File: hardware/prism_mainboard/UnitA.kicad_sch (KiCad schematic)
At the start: 8 parts, among them U1 XC7Z010-1CLG400C

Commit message: KiCAD Update
Added Power System Schematics. Decided on a 4 in 1 Buck and LDO, LP87222TQ1, for 3.3V and 1.8V LDO, and 1.8V and 1.0V Buck converter.
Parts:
- U1: footprint CLG400_XIL -> XC7Z010-1CLG400C:CLG400_XIL

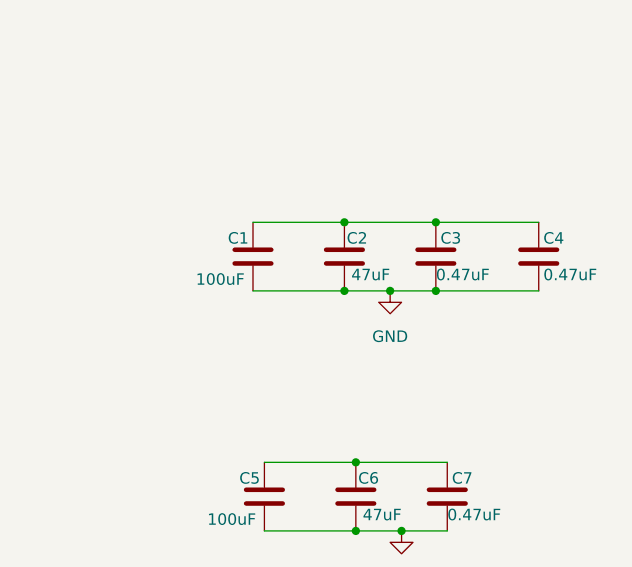
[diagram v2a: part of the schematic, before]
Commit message: Schematics
More schematics updates, moving to Desktop for editing. Continued with power usage, debating use of Dedicated DDR3/3L power IC instead of using LDO and Buck from mainboard power.
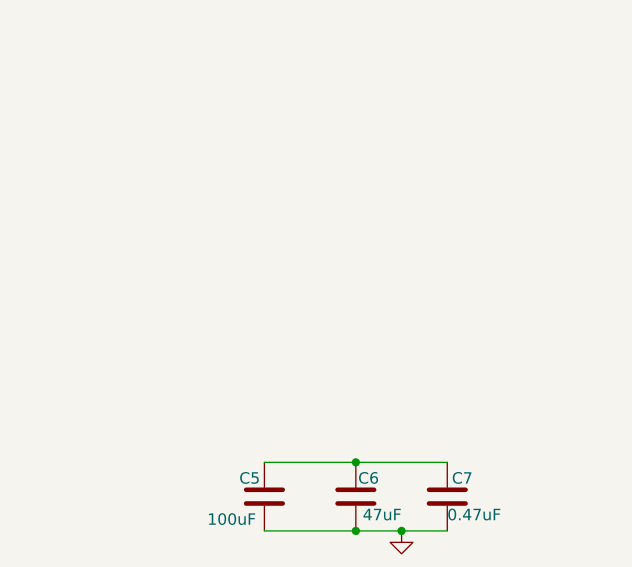
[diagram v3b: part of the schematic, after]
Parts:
- removed C1: 100uF, symbol Device:C
- removed C2: 47uF, symbol Device:C
- removed C3, C4: 0.47uF, symbol Device:C

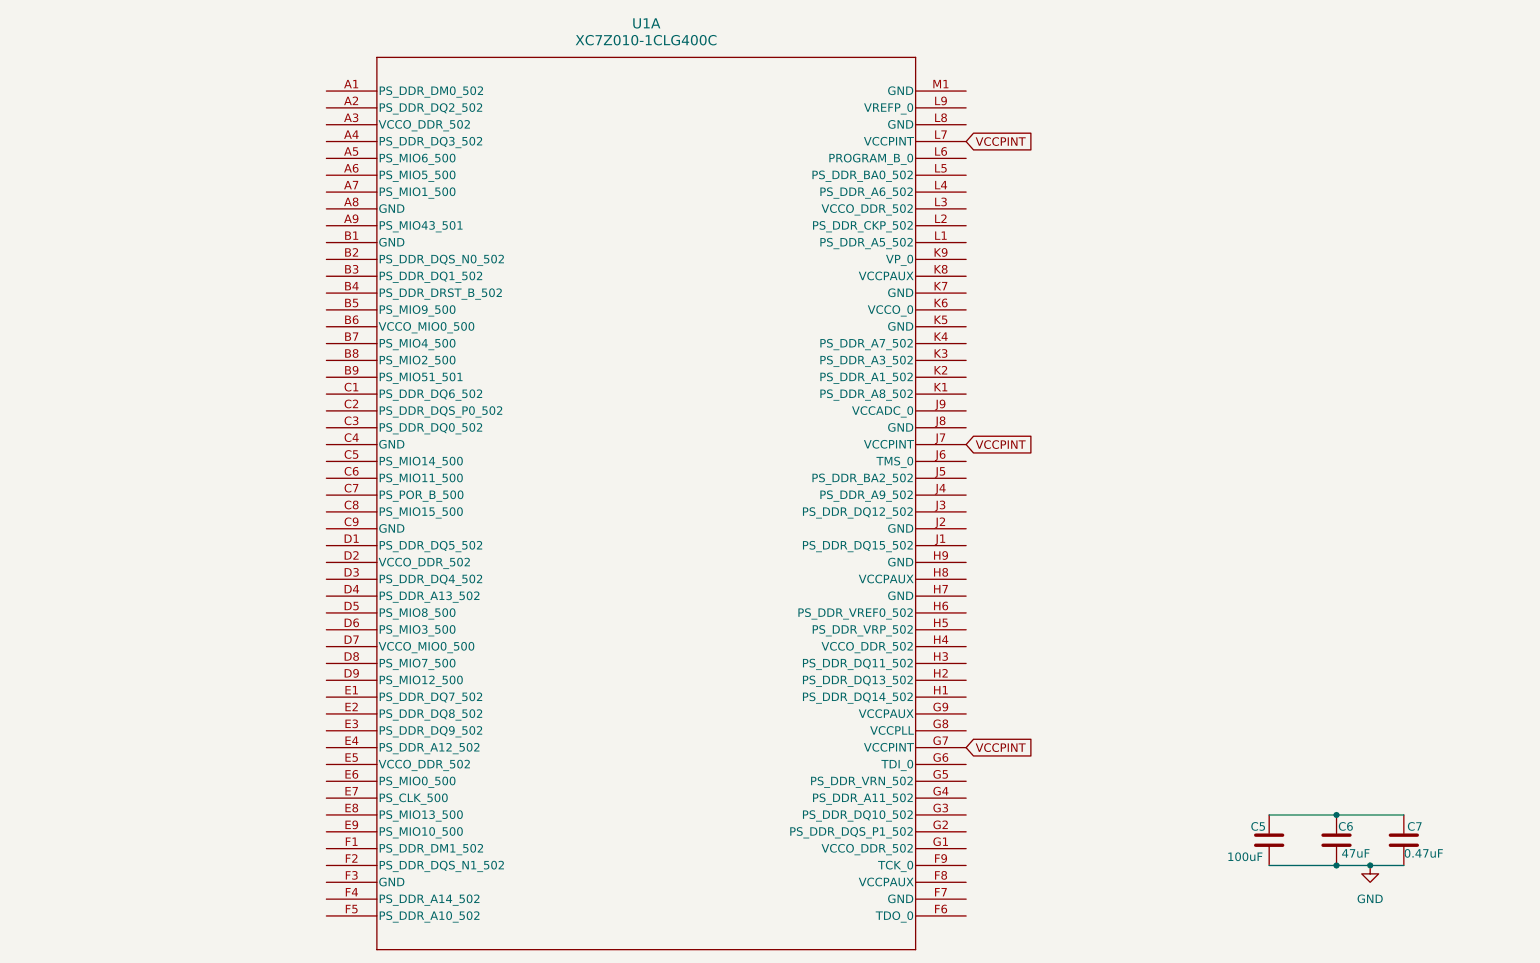
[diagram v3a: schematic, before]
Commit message: Power System Schematics
Updated Power System Schematics, changed the power supply IC from 2 Buck 2 LDO to 4 Buck and include 2 LDO to provide Low Noise power to RF and sensitive circuitry
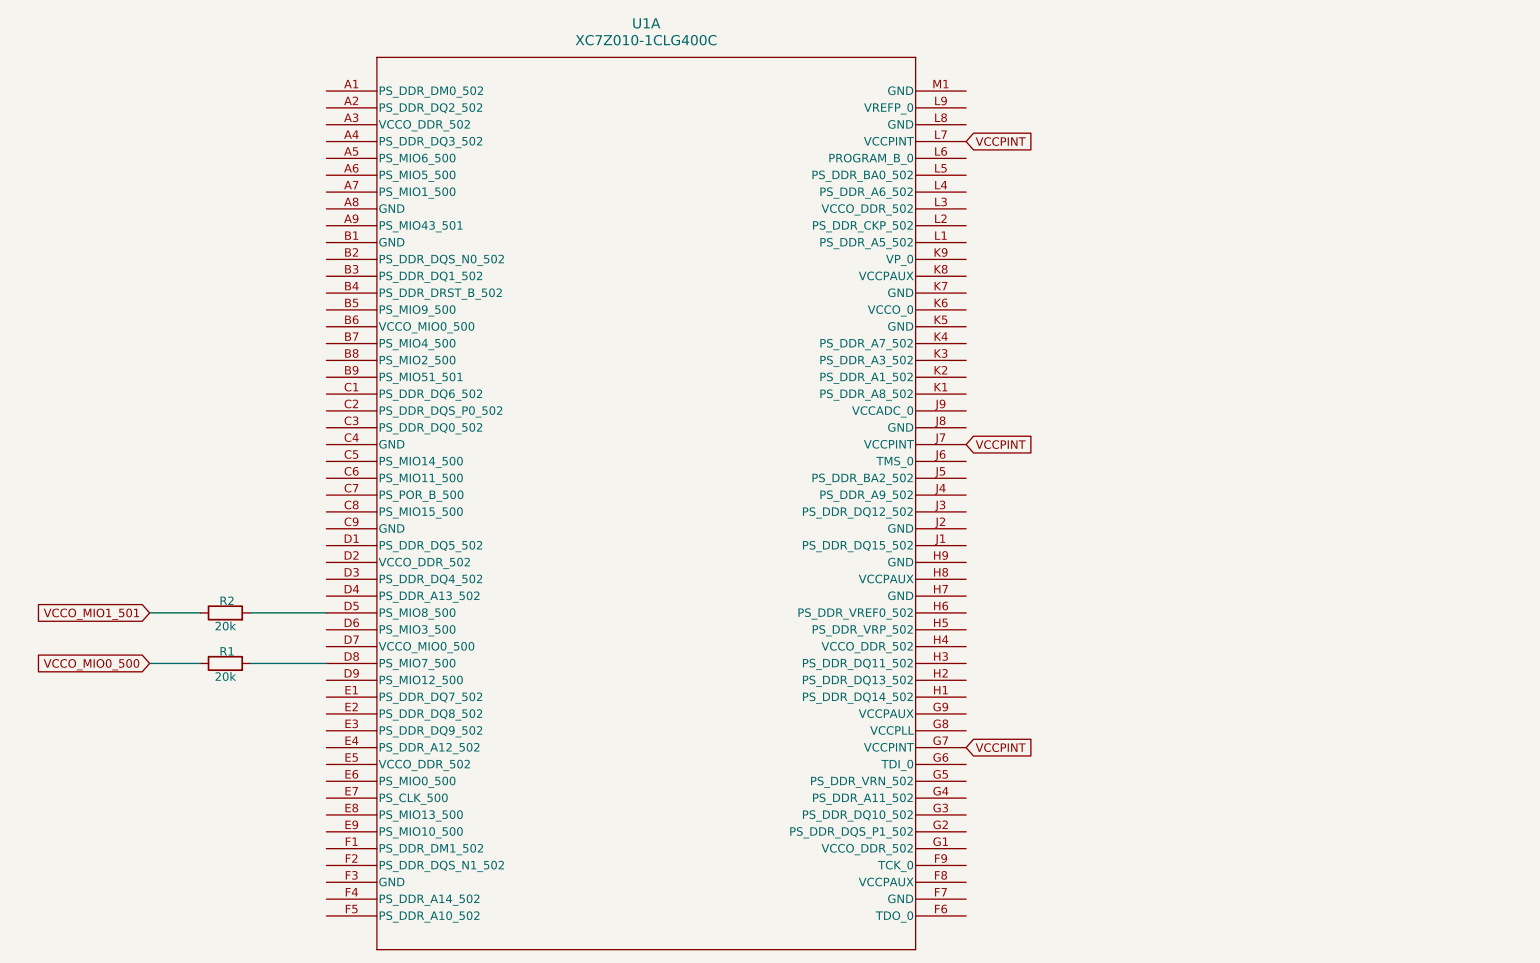
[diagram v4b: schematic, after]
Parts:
- removed C5: 100uF, symbol Device:C
- removed C6: 47uF, symbol Device:C
- removed C7: 0.47uF, symbol Device:C
- added R1, R2: 20k, symbol Device:R
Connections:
- net at U1.D5 (PS_MIO8_500): now also R2.2
- net at U1.D8 (PS_MIO7_500): now also R1.2
- new net VCCO_MIO0_500: R1.1
- new net VCCO_MIO1_501: R2.1
